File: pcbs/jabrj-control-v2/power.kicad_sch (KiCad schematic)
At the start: 0 parts

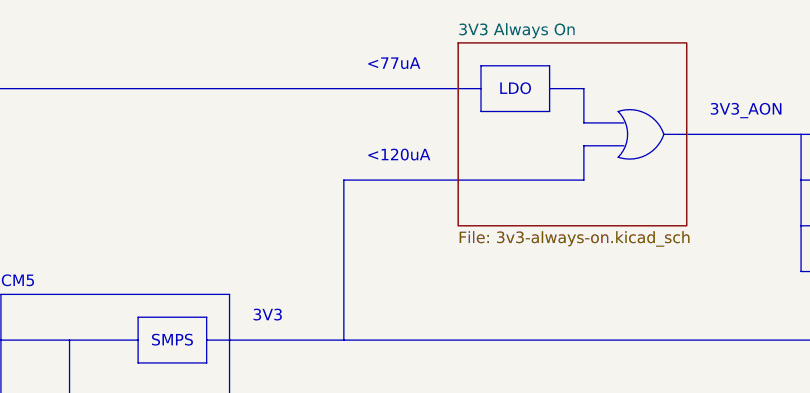
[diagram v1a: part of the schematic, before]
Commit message: Minor schematic fixes
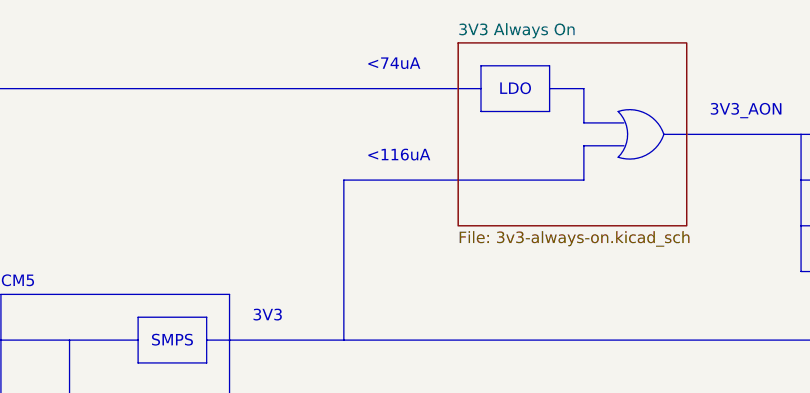
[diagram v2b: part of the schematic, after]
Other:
- note added: "<116uA"
- note added: "<74uA"
- note removed: "<120uA"
- note removed: "<77uA"
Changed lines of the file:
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@@
 		)
 	)
-	(text "<77uA"
+	(text "<74uA"
 		(exclude_from_sim no)
 		(at 180.34 43.18 0)
@@
 		)
 	)
-	(text "<120uA"
+	(text "<116uA"
 		(exclude_from_sim no)
 		(at 180.34 53.34 0)

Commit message: 603 Unrouted
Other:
- sheet Power In ports: added {I2C}; removed none
- note added: "200mA"
- note added: "Fan"
